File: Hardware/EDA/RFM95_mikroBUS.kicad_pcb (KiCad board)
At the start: 4 copper layers, 25.4 x 28.6 mm, 7 parts, among them J1 u.FL, J2 SMA, P1 HEADER_M_2.54MM_1R8P_ST_AU_PTH, P2 HEADER_M_2.54MM_1R8P_ST_AU_PTH, U1 RFM95W

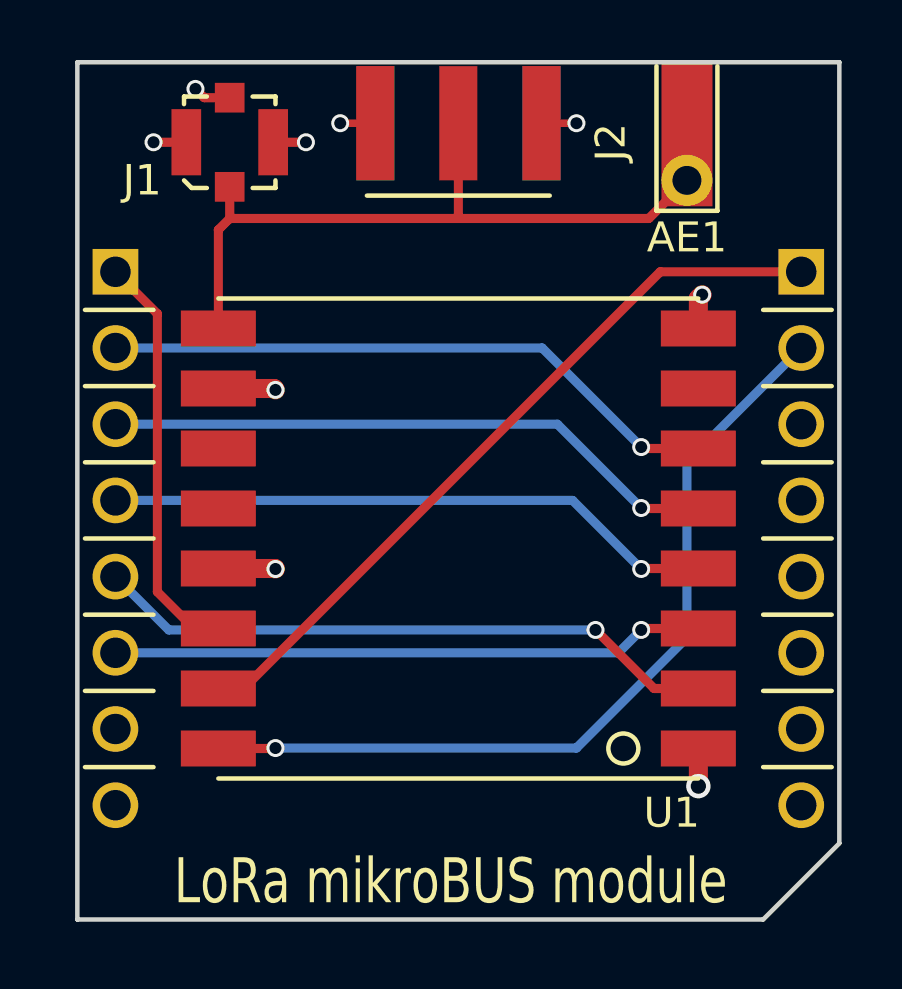
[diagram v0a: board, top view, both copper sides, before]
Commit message: Changed name from LoRa mikroBUS to RFM95 mikroBUS.  Added zero ohm resistor and solder links for RF path and DIO configuration options.
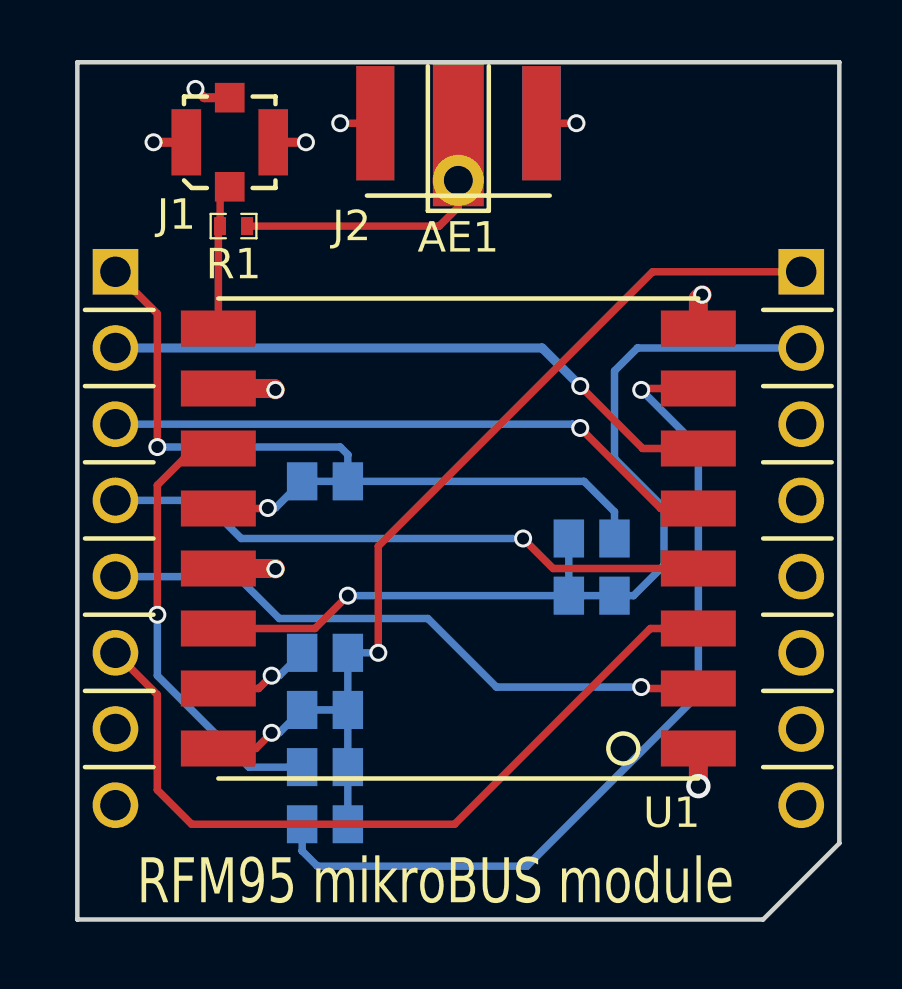
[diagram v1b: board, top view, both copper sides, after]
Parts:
- added LK1: NO, Passive:SOLDER_LINK_NO, B.Cu at (119.3, 117.5)
- added LK2: NC, Passive:SOLDER_LINK_NC, B.Cu at (119.3, 119.4)
- added LK3: NO, Passive:SOLDER_LINK_NO, B.Cu at (119.3, 121.3)
- added LK4: NO, Passive:SOLDER_LINK_NO, B.Cu at (119.3, 123.2)
- added LK5: NC, Passive:SOLDER_LINK_NC, B.Cu at (119.3, 111.8)
- added LK6: NO, Passive:SOLDER_LINK_NO, B.Cu at (128.1, 113.7)
- added LK7: NC, Passive:SOLDER_LINK_NC, B.Cu at (128.1, 115.6)
- added R1: DNP, Passive:0402, F.Cu at (116.2, 103.3)
- AE1: value Antenna -> Antenna_Helical_RA
- moved AE1 7.62 mm to (123.7, 101.7)
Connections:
- J1 pad 1: Net-(AE1-Pad1) -> Net-(J1-Pad1)
- U1 pad 11: Net-(U1-Pad11) -> DIO3
- U1 pad 12: Net-(U1-Pad12) -> DIO4
- U1 pad 14: AN -> DIO0
- U1 pad 15: PWM -> DIO1
- U1 pad 16: INT -> DIO2
- U1 pad 7: Net-(U1-Pad7) -> DIO5
- U1 pad 9: Net-(AE1-Pad1) -> Net-(J1-Pad1)
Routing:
- net DIO5: track 0.00 -> 29.5 mm, vias 0 -> 1
- net Net-(AE1-Pad1): track 23.8 -> 8.20 mm
- net DIO3: track 0.00 -> 15.0 mm, vias 0 -> 1
- net DIO0: track 0.00 -> 14.9 mm, vias 0 -> 1
- net INT: track 28.4 -> 15.8 mm, vias 1 -> 0
- net AN: track 13.8 -> 24.0 mm, vias 0 -> 1
- net MOSI: track 19.8 -> 26.4 mm, vias 1 -> 0
- net Net-(J1-Pad1): track 0.00 -> 4.88 mm
- net DIO1: track 0.00 -> 4.38 mm, vias 0 -> 1
- net DIO2: track 0.00 -> 3.33 mm, vias 0 -> 1
- net DIO4: track 0.00 -> 3.19 mm, vias 0 -> 1
- net PWM: track 25.4 -> 28.2 mm, vias 0 -> 1
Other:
- board text added: "RFM95 mikroBUS module"
- board text removed: "LoRa mikroBUS module"

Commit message: Peer-review package
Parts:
- removed R1: DNP, Passive:0402
- moved LK7 9.67 mm to (119.3, 111.8)
- moved LK6 9.09 mm to (128.1, 113.7)
- moved LK5 1.90 mm to (128.1, 115.6)
- renumbered LK6 to LK5, LK5 to LK6
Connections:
- J1 pad 1: Net-(J1-Pad1) -> Net-(AE1-Pad1)
- U1 pad 9: Net-(J1-Pad1) -> Net-(AE1-Pad1)
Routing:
- net DIO4: track 3.19 -> 12.1 mm
- net DIO0: track 14.9 -> 22.4 mm, vias 1 -> 2
- net Net-(AE1-Pad1): track 8.20 -> 13.5 mm
- net Net-(J1-Pad1): track 4.88 -> 0.00 mm
- net PWM: track 28.2 -> 32.4 mm
- net INT: track 15.8 -> 18.1 mm
- net AN: track 24.0 -> 25.7 mm
- net DIO1: track 4.38 -> 3.29 mm
- net SCK: track 20.4 -> 21.1 mm

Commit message: Added several files. Final release and boards ordered from OSHPark.
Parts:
- moved J1 0.41 mm to (115.7, 100.6)
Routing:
- net PWM: track 32.4 -> 28.1 mm
- net Net-(AE1-Pad1): track 13.5 -> 16.5 mm

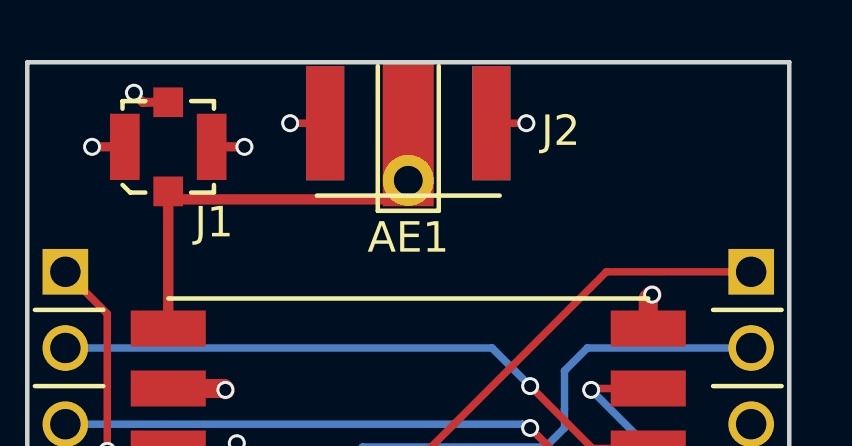
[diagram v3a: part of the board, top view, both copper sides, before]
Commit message: Corrected SMA Edge connector footprint and regenerated gerber files.
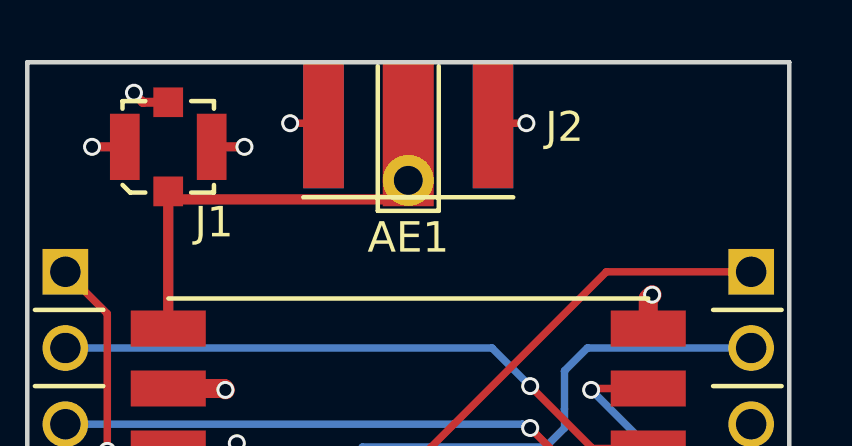
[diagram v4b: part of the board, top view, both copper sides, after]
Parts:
- moved J2 0.13 mm to (123.7, 97.8)
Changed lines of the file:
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@@
     (46 B.CrtYd user)
     (47 F.CrtYd user)
-    (48 B.Fab user)
-    (49 F.Fab user)
+    (48 B.Fab user hide)
+    (49 F.Fab user hide)
   )
   (setup
@@
     (visible_elements 7FFEFFFF)
     (pcbplotparams
-      (layerselection 0x311fc_80000007)
+      (layerselection 0x011fc_80000007)
       (usegerberextensions false)
       (excludeedgelayer false)
       (linewidth 0.100000)
-      (plotframeref true)
+      (plotframeref false)
       (viasonmask false)
       (mode 1)
-      (useauxorigin false)
+      (useauxorigin true)
       (hpglpennumber 1)
       (hpglpenspeed 20)
@@
       (padsonsilk false)
       (subtractmaskfromsilk false)
-      (outputformat 4)
+      (outputformat 1)
       (mirror false)
       (drillshape 0)
       (scaleselection 1)
-      (outputdirectory Z:/Engineering/Projects/mikroBUS_Modules/RFM95_mikroBUS/Hardware/EDA/PCB_Assembly/))
+      (outputdirectory Z:/Engineering/Projects/mikroBUS_Modules/RFM95_mikroBUS/Hardware/EDA/Gerbers/))
   )
   (net 0 "")
@@
     (pad 1 smd rect (at 0 -1.524) (size 1.7018 4.7752) (layers F.Cu F.Mask)
       (net 16 "Net-(AE1-Pad1)"))
-  )
-  (module Connector:SMA_EDGE (layer F.Cu)
-    (at 123.698 97.917 270)
-    (attr smd)
-    (fp_text reference J2 (at 2.159 -5.08 360) (layer F.SilkS)
-      (effects (font (size 1.016 1.016) (thickness 0.2032)))
-    )
-    (fp_text value SMA (at 3.81 5.08 270) (layer F.Fab)
-      (effects (font (size 1 1) (thickness 0.15)))
-    )
-    (fp_line (start 4.318 -3.048) (end 4.318 3.048) (layer F.SilkS) (width 0.15))
-    (pad "" smd rect (at 1.905 2.7686 270) (size 3.81 1.27) (layers B.Cu))
-    (pad "" smd rect (at 1.905 -2.7686 270) (size 3.81 1.27) (layers B.Cu))
-    (pad 2 smd rect (at 1.905 -2.7686 270) (size 3.81 1.27) (layers F.Cu)
-      (net 7 GND))
-    (pad 3 smd rect (at 1.905 2.7686 270) (size 3.81 1.27) (layers F.Cu)
-      (net 7 GND))
-    (pad 1 smd rect (at 1.905 0 270) (size 3.81 1.27) (layers F.Cu F.Paste F.Mask)
-      (net 16 "Net-(AE1-Pad1)"))
-    (model C:/Engineering/KiCAD_Libraries/3D/Connectors/RF/VRML/SMA_EDGE.wrl
-      (at (xyz 0 0 0))
-      (scale (xyz 1 1 1))
-      (rotate (xyz 0 0 0))
-    )
   )
   (module Passive:SOLDER_LINK_NC (layer B.Cu)
@@
     (fp_line (start 0.640717 -1.782296) (end 1.288614 -1.782296) (layer B.SilkS) (width 0.1))
   )
+  (module Connector:SMA_EDGE (layer F.Cu)
+    (at 123.698 97.79 270)
+    (fp_text reference J2 (at 2.159 -5.207 360) (layer F.SilkS)
+      (effects (font (size 1 1) (thickness 0.15)))
+    )
+    (fp_text value SMA (at 2.1 4.5 270) (layer F.Fab)
+      (effects (font (size 1 1) (thickness 0.15)))
+    )
+    (fp_text user "PCB Edge" (at 3.1 -5 270) (layer F.Fab)
+      (effects (font (size 0.5 0.5) (thickness 0.1)))
+    )
+    (fp_line (start 0.2 -3.8) (end 1.2 -4.7) (layer F.Fab) (width 0.127))
+    (fp_line (start 0.2 -3.8) (end 0.7 -4) (layer F.Fab) (width 0.127))
+    (fp_line (start 0.2 -3.8) (end 0.4 -4.2) (layer F.Fab) (width 0.127))
+    (fp_line (start 0 -3.5) (end 0 3.5) (layer F.Fab) (width 0.127))
+    (fp_line (start 4.5 -3.5) (end 4.5 3.5) (layer F.SilkS) (width 0.15))
+    (pad "" connect rect (at 2.1 2.825 270) (size 4.2 1.35) (layers B.Cu B.Mask))
+    (pad "" connect rect (at 2.1 -2.825 270) (size 4.2 1.35) (layers B.Cu B.Mask))
+    (pad 2 connect rect (at 2.1 -2.825 270) (size 4.2 1.35) (layers F.Cu F.Mask)
+      (net 7 GND))
+    (pad 3 connect rect (at 2.1 2.825 270) (size 4.2 1.35) (layers F.Cu F.Mask)
+      (net 7 GND))
+    (pad 1 connect rect (at 1.9 0 270) (size 3.6 1.27) (layers F.Cu F.Mask)
+      (net 16 "Net-(AE1-Pad1)"))
+    (model C:/Engineering/KiCAD_Libraries/3D/Connectors/RF/VRML/SMA_EDGE.wrl
+      (at (xyz 0 0 0))
+      (scale (xyz 1 1 1))
+      (rotate (xyz 0 0 0))
+    )
+  )
   (dimension 25.4 (width 0.3) (layer Dwgs.User)
     (gr_text "1.0000 in" (at 123.698 92.63) (layer Dwgs.User)
@@
   (via (at 117.602 114.681) (size 0.6) (drill 0.4) (layers F.Cu B.Cu) (net 6))
   (segment (start 117.586 114.665) (end 117.602 114.681) (width 0.635) (layer F.Cu) (net 6))
+  (via (at 119.761 99.822) (size 0.6) (drill 0.4) (layers F.Cu B.Cu) (net 7))
+  (segment (start 120.9294 99.822) (end 119.761 99.822) (width 0.25) (layer F.Cu) (net 7))
   (segment (start 131.698 106.665) (end 131.698 105.665) (width 0.635) (layer F.Cu) (net 7))
   (via (at 131.826 105.537) (size 0.6) (drill 0.4) (layers F.Cu B.Cu) (net 7))
@@
   (segment (start 126.4666 99.822) (end 127.635 99.822) (width 0.25) (layer F.Cu) (net 7))
   (via (at 127.635 99.822) (size 0.6) (drill 0.4) (layers F.Cu B.Cu) (net 7))
-  (segment (start 120.9294 99.822) (end 119.761 99.822) (width 0.25) (layer F.Cu) (net 7))
-  (via (at 119.761 99.822) (size 0.6) (drill 0.4) (layers F.Cu B.Cu) (net 7))
   (segment (start 117.1448 100.6094) (end 118.237 100.6094) (width 0.3048) (layer F.Cu) (net 7))
   (via (at 118.237 100.6094) (size 0.6) (drill 0.4) (layers F.Cu B.Cu) (net 7))

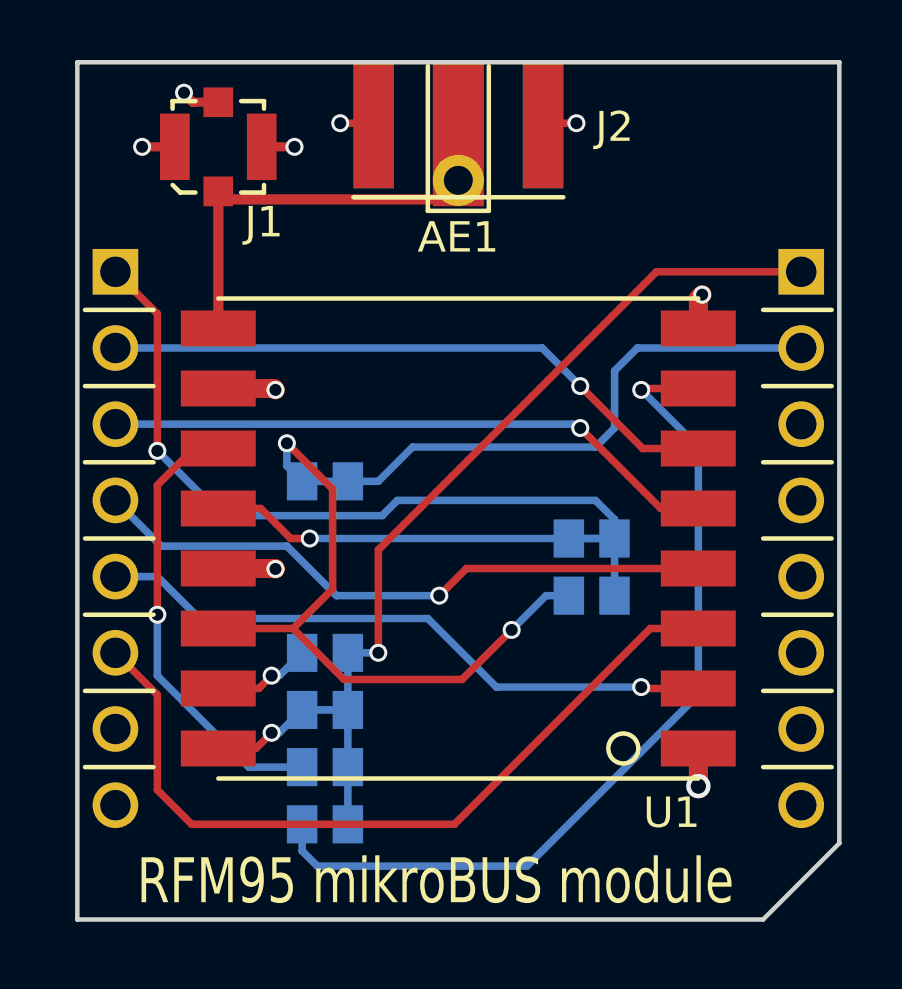
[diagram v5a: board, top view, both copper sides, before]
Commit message: Added logo to silkscreen and standardized ref des sizes.
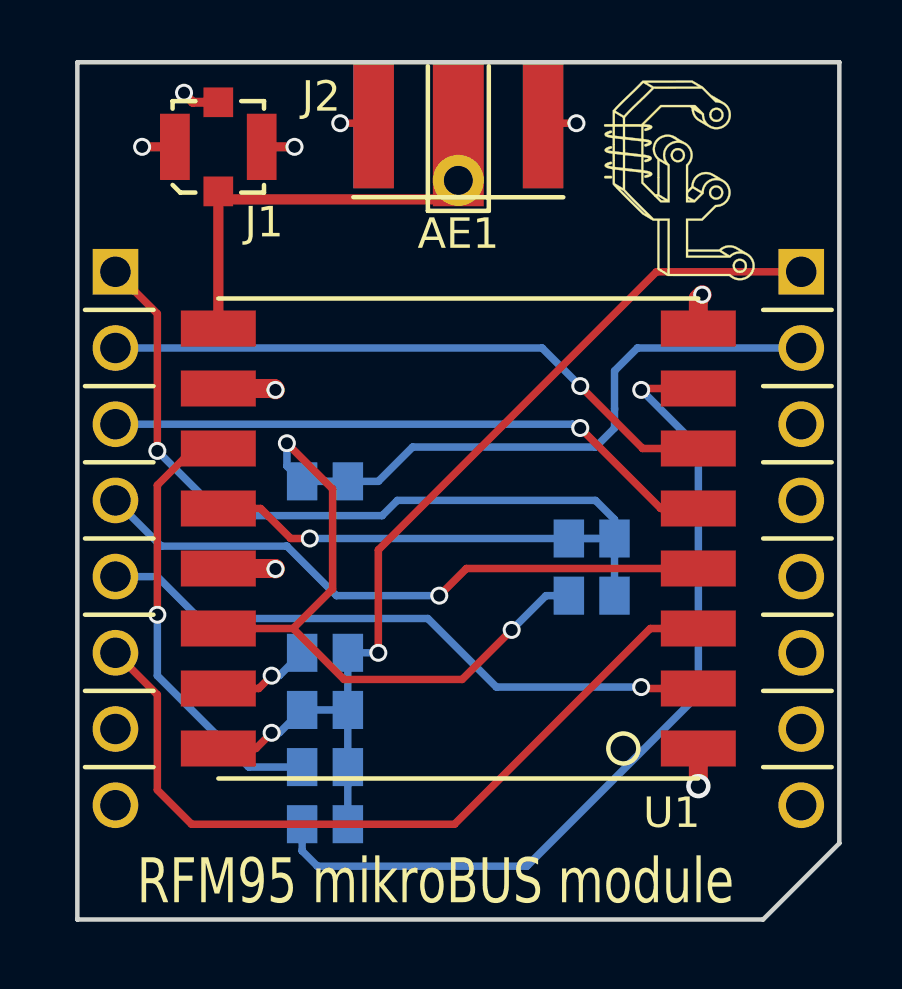
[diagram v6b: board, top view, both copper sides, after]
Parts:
- added G1: Casco_Logix_Logo, Logo:Casco_Logix_Logo_6x6MM, F.Cu at (131.1, 101.7)
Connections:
- P2 pad 3: RX -> (no net)
- P2 pad 4: TX -> (no net)
- P2 pad 5: SCL -> (no net)
- P2 pad 6: SDA -> (no net)
- P2 pad 7: +5V -> (no net)
